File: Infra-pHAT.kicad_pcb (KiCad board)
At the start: 2 copper layers, 65 x 30 mm, 24 parts, among them Q1 BC817

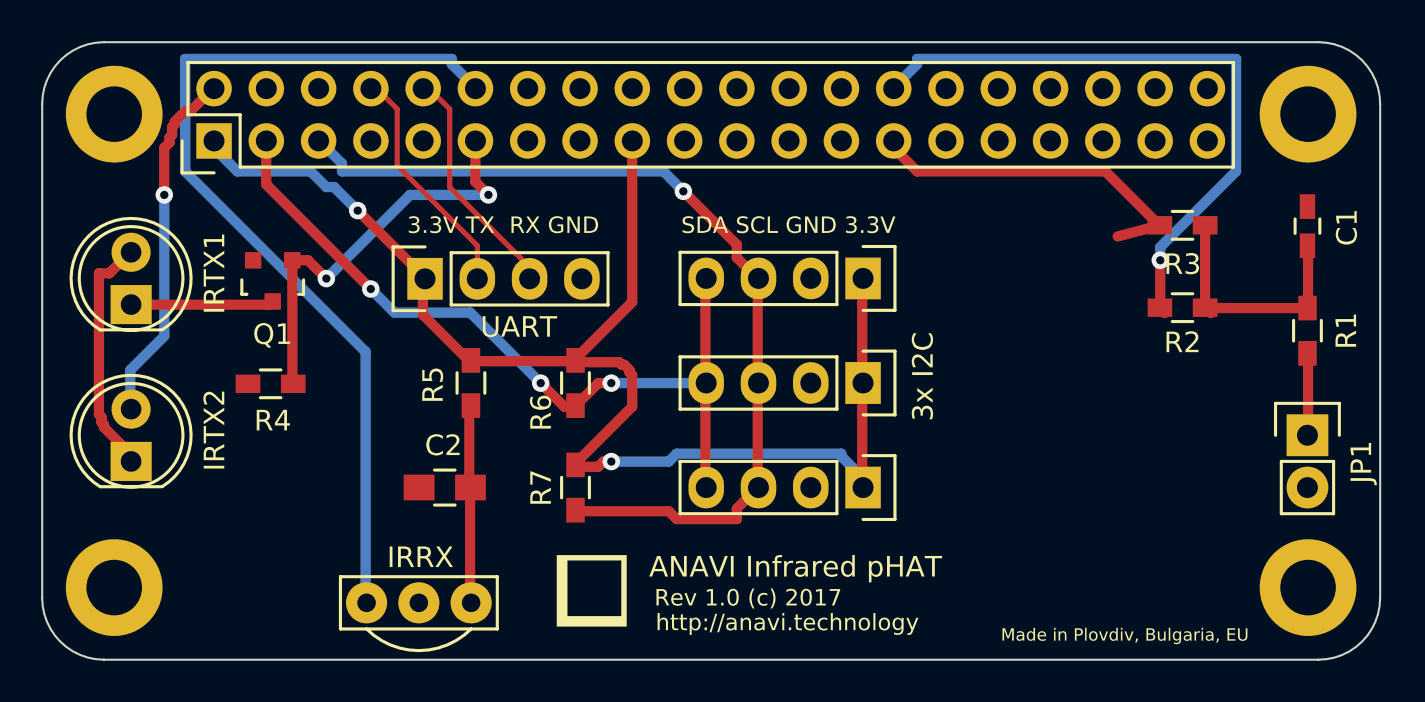
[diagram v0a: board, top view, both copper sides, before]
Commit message: placed the footprint for CAT24C32WI-GT3 & deleted the UART connector
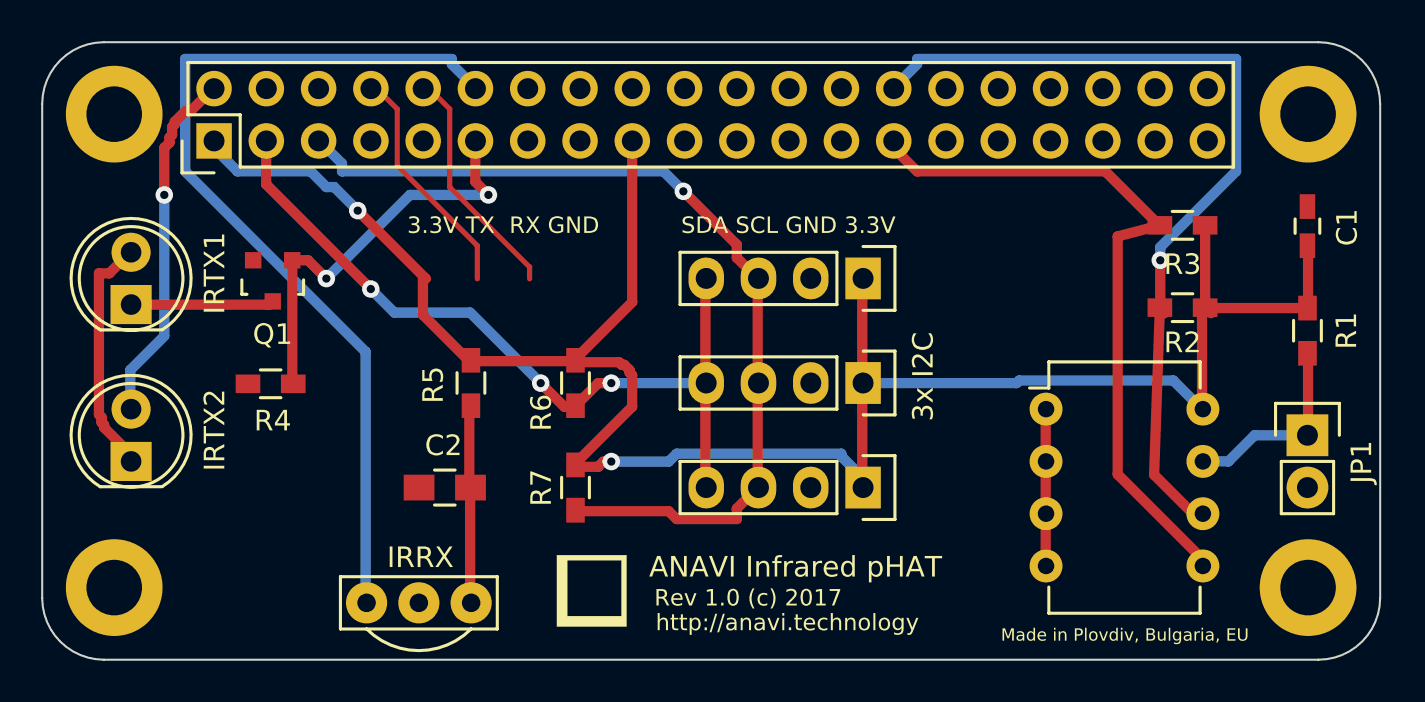
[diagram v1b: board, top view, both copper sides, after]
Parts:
- removed UART: CONN_01X04, Pin_Headers:Pin_Header_Straight_1x04
- added U1: CAT24C32WI-GT3, Housings_DIP:DIP-8_W7.62mm, F.Cu at (197.3, 92.8)
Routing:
- net +3V3: track 83.4 -> 105.5 mm
- net Net-(R3-Pad2): track 17.2 -> 35.1 mm
- net Net-(R2-Pad2): track 31.4 -> 42.8 mm
- net GND: track 0.00 -> 8.40 mm
- net Net-(JP1-Pad1): track 4.33 -> 10.1 mm
